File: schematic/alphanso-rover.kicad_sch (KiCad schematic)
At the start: 11 parts, among them M1 TT Motor (Adafruit #3777), M2 TT Motor (Adafruit #3777), M3 TT Motor (Adafruit #3777), M4 TT Motor (Adafruit #3777), U1 ESP32-DEVKIT-V1, U2 TB6612FNG, U3 TB6612FNG, U4 LM2596S-5

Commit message: updated schematic and gitignore
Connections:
- net +5V: now also U3.19 (STBY)
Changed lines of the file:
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@@
+	)
+	(junction
+		(at 173.99 104.14)
+		(diameter 0)
+		(color 0 0 0 0)
 	)
 	(junction
@@
 	(wire
 		(pts
+			(xy 217.17 104.14) (xy 173.99 104.14)
+		)
+		(stroke
+			(width 0)
+			(type default)
+		)
+	)
+	(wire
+		(pts
 			(xy 63.5 152.4) (xy 63.5 161.29)
 		)
@@
 	(wire
 		(pts
+			(xy 217.17 100.33) (xy 217.17 104.14)
+		)
+		(stroke
+			(width 0)
+			(type default)
+		)
+	)
+	(wire
+		(pts
 			(xy 66.04 158.75) (xy 66.04 152.4)
 		)
@@
 	(wire
 		(pts
-			(xy 173.99 92.71) (xy 173.99 177.8)
+			(xy 173.99 92.71) (xy 173.99 104.14)
 		)
 		(stroke
@@
 		)
 		(stroke
+			(width 0)
+			(type default)
+		)
+	)
+	(wire
+		(pts
+			(xy 173.99 104.14) (xy 173.99 177.8)
+		)
+		(stroke

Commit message: initialized platformio
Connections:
- net at U1.10 (D19): now also U2.15 (PWMB)
- net at U1.11 (D21): now also U2.23 (PWMA); no longer R1.1
- net at U1.26 (D14): now also U2.22 (AIN2); no longer U2.15 (PWMB)
- net at U1.27 (D12): no longer U2.22 (AIN2)
- net at U1.28 (D13): now also U2.17 (BIN1); no longer U2.21 (AIN1)
- net at U1.4 (D2): now also R1.1
- net at U1.8 (D5): no longer U2.17 (BIN1)
- net at U1.9 (D18): now also U2.21 (AIN1); no longer U2.23 (PWMA)
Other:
- moved on the sheet: D1, R1

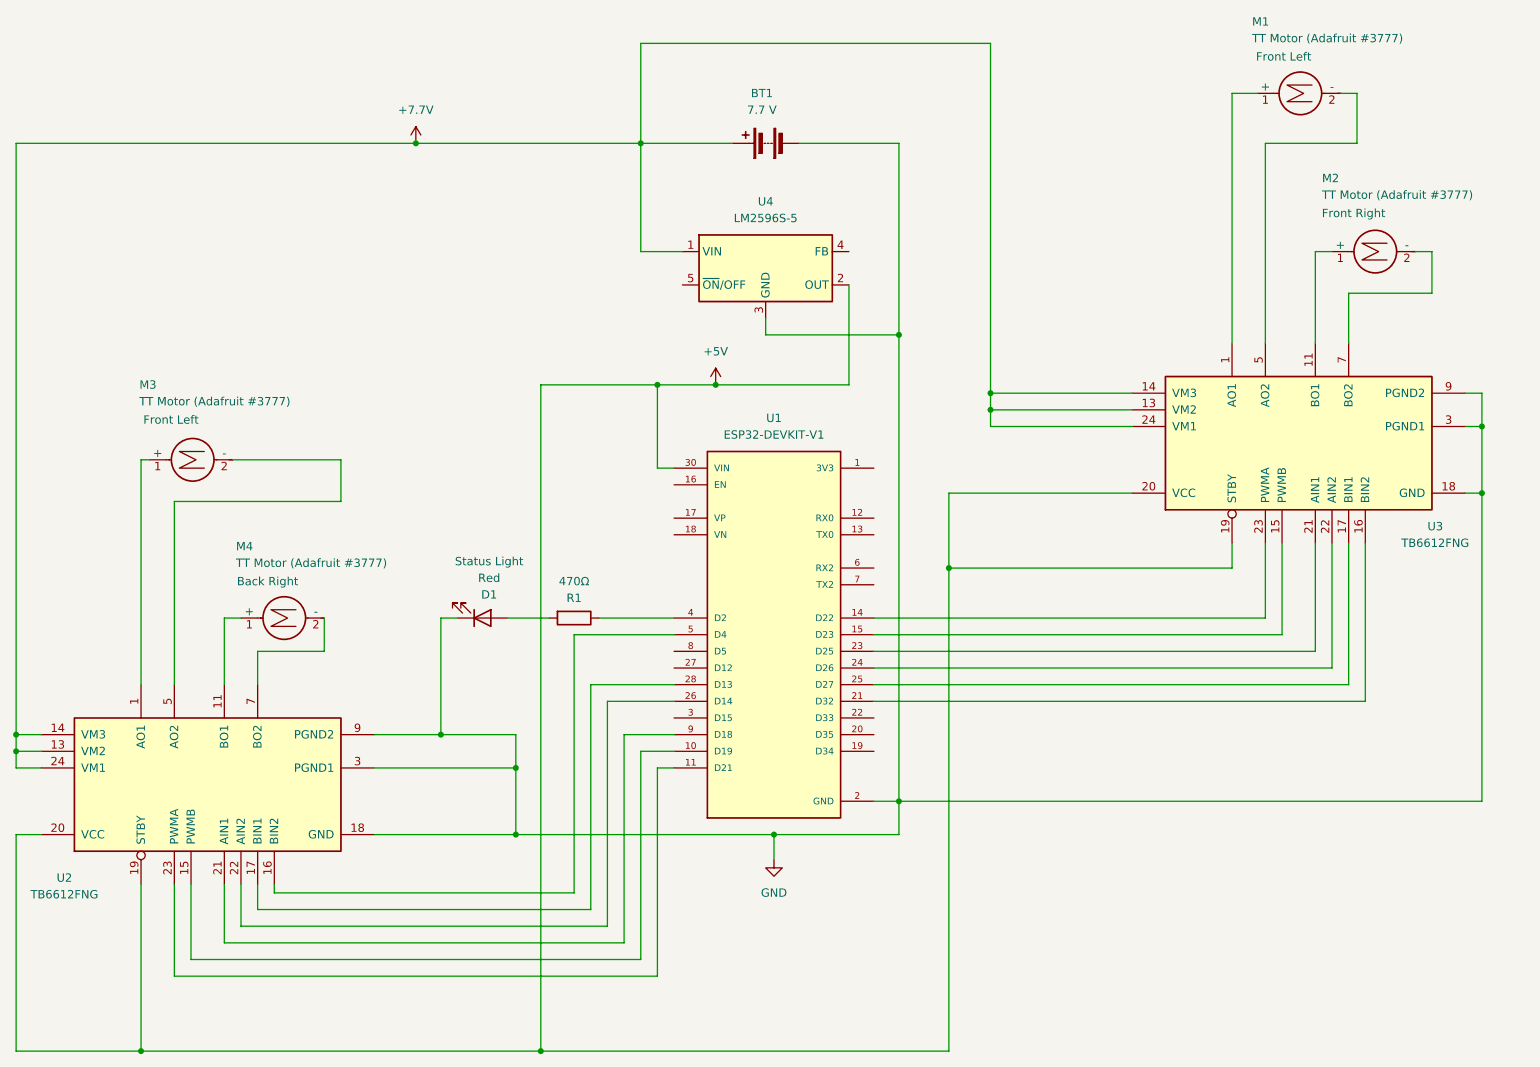
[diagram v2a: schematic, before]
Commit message: added all motors
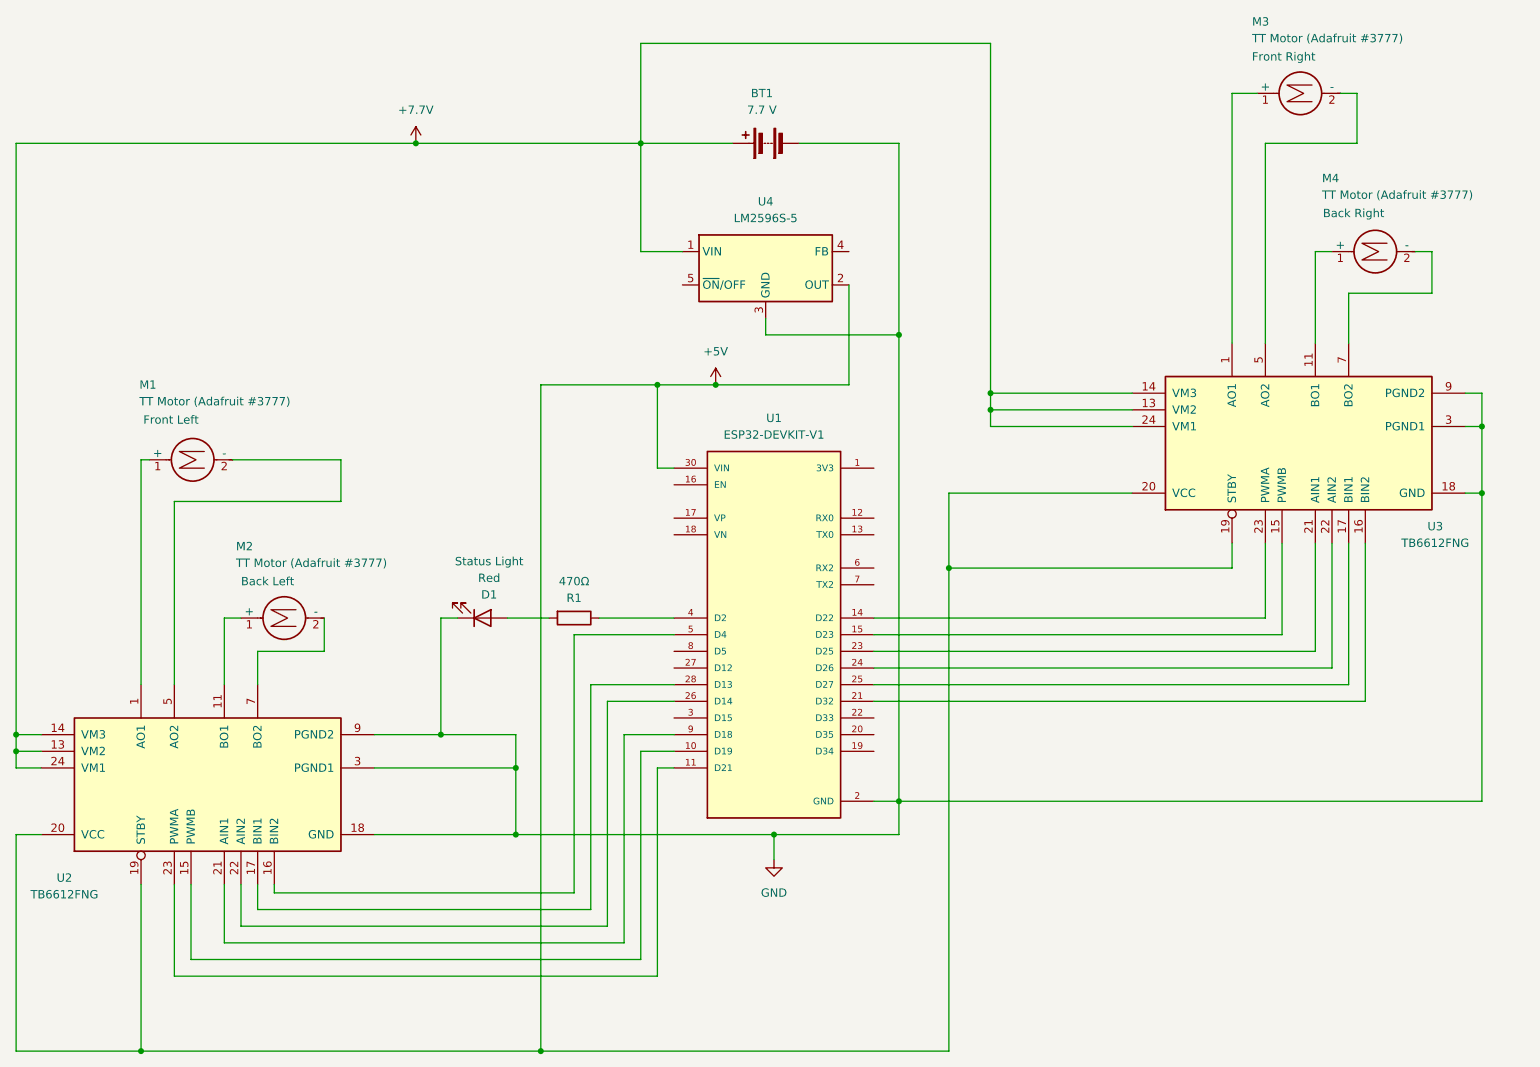
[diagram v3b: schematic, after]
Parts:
- renumbered M3 to M1, M4 to M2, M1 to M3, M2 to M4
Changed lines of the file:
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@@
 	(title_block
 		(title "Alphanso Rover")
-		(date "2026-05-31")
+		(date "2026-06-08")
 		(rev "1")
 	)
@@
 		(on_board yes)
 		(dnp no)
-		(property "Reference" "M3"
+		(property "Reference" "M1"
 			(at 50.546 76.1999 90)
 			(effects
@@
 			(project "alphanso-rover"
 				(path "/f6d5d2e9-435d-48e8-a1b3-a68604a4dfea"
-					(reference "M3")
+					(reference "M1")
 					(unit 1)
 				)
@@
 		(on_board yes)
 		(dnp no)
-		(property "Reference" "M1"
+		(property "Reference" "M3"
 			(at 220.218 20.8279 90)
 			(effects
@@
 			)
 		)
-		(property "Description" "Front Left"
+		(property "Description" "Front Right"
 			(at 225.044 26.162 90)
 			(effects
@@
 			(project "alphanso-rover"
 				(path "/f6d5d2e9-435d-48e8-a1b3-a68604a4dfea"
-					(reference "M1")
+					(reference "M3")
 					(unit 1)
 				)
@@
 		(on_board yes)
 		(dnp no)
-		(property "Reference" "M4"
+		(property "Reference" "M2"
 			(at 65.278 100.8379 90)
 			(effects
@@
 			)
 		)
-		(property "Description" "Back Right"
+		(property "Description" "Back Left"
 			(at 70.104 106.172 90)
 			(effects
@@
 			(project "alphanso-rover"
 				(path "/f6d5d2e9-435d-48e8-a1b3-a68604a4dfea"
-					(reference "M4")
+					(reference "M2")
 					(unit 1)
 				)
@@
 		(on_board yes)
 		(dnp no)
-		(property "Reference" "M2"
+		(property "Reference" "M4"
 			(at 230.886 44.7039 90)
 			(effects
@@
 			)
 		)
-		(property "Description" "Front Right"
+		(property "Description" "Back Right"
 			(at 235.712 50.038 90)
 			(effects
@@
 			(project "alphanso-rover"
 				(path "/f6d5d2e9-435d-48e8-a1b3-a68604a4dfea"
-					(reference "M2")
+					(reference "M4")
 					(unit 1)
 				)
